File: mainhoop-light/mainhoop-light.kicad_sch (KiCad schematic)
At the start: 69 parts, among them IC1 BCR420U, IC3 BCR420U, IC4 BCR420U, IC5 BCR420U, IC6 BCR420U, J1 Conn_01x04, Q1 2N7002, Q12 Si2301CDS, Q13 2N7002, Q14 2N7002, Q15 Si2301CDS, Q16 2N7002, Q2 2N7002, Q3 Si2301CDS, Q7 2N7002, U1 AP2204K-ADJ, U2 SE555D

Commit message: Add files via upload
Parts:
- added R11, R12, R13: 10k, Resistor_SMD:R_0603_1608Metric, symbol Device:R_Small
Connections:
- net GND: now also R11.1, R12.1, R13.1
- net GREEN_EN: now also R11.2
- net RED_EN: now also R12.2
- net at Q2.1 (G): now also Q1.3 (D), R1.1
- net TSAL renamed RTML
- net TSAL_EN renamed RTML_EN
- net RTML_EN: now also R13.2
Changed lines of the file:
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@@
     (company "NCKU Formula Racing")
   )
+  (junction (at 200.66 152.4) (diameter 0) (color 0 0 0 0)
+  )
   (junction (at 59.055 35.56) (diameter 0) (color 0 0 0 0)
   )
@@
   (junction (at 69.85 41.91) (diameter 0) (color 0 0 0 0)
   )
+  (junction (at 171.45 152.4) (diameter 0) (color 0 0 0 0)
+  )
+  (junction (at 200.66 125.73) (diameter 0) (color 0 0 0 0)
+  )
   (junction (at 67.945 76.835) (diameter 0) (color 0 0 0 0)
   )
@@
   (junction (at 67.945 70.485) (diameter 0) (color 0 0 0 0)
   )
+  (junction (at 71.12 184.15) (diameter 0) (color 0 0 0 0)
+  )
   (junction (at 40.005 135.255) (diameter 0) (color 0 0 0 0)
   )
@@
     (stroke (width 0) (type default))
   )
+  (wire (pts (xy 171.45 152.4) (xy 162.56 152.4))
+    (stroke (width 0) (type default))
+  )
   (wire (pts (xy 211.455 48.26) (xy 211.455 53.34))
     (stroke (width 0) (type default))
@@
     (stroke (width 0) (type default))
   )
+  (wire (pts (xy 220.98 152.4) (xy 200.66 152.4))
+    (stroke (width 0) (type default))
+  )
   (wire (pts (xy 198.12 71.755) (xy 198.12 74.295))
     (stroke (width 0) (type default))
@@
     (stroke (width 0) (type default))
   )
+  (wire (pts (xy 220.98 137.16) (xy 220.98 152.4))
+    (stroke (width 0) (type default))
+  )
   (wire (pts (xy 211.455 97.79) (xy 211.455 102.87))
     (stroke (width 0) (type default))
@@
     (stroke (width 0) (type default))
   )
+  (wire (pts (xy 171.45 137.16) (xy 171.45 152.4))
+    (stroke (width 0) (type default))
+  )
   (wire (pts (xy 200.66 116.84) (xy 212.09 116.84))
     (stroke (width 0) (type default))
@@
     (stroke (width 0) (type default))
   )
+  (wire (pts (xy 204.47 137.16) (xy 204.47 125.73))
+    (stroke (width 0) (type default))
+  )
   (wire (pts (xy 171.45 116.84) (xy 171.45 119.38))
     (stroke (width 0) (type default))
@@
     (stroke (width 0) (type default))
   )
+  (wire (pts (xy 85.09 186.69) (xy 74.93 186.69))
+    (stroke (width 0) (type default))
+  )
   (wire (pts (xy 69.85 35.56) (xy 69.85 36.195))
     (stroke (width 0) (type default))
   )
+  (wire (pts (xy 74.93 186.69) (xy 74.93 184.15))
+    (stroke (width 0) (type default))
+  )
   (wire (pts (xy 73.025 145.415) (xy 69.85 145.415))
     (stroke (width 0) (type default))
@@
     (stroke (width 0) (type default))
   )
+  (wire (pts (xy 74.93 184.15) (xy 71.12 184.15))
+    (stroke (width 0) (type default))
+  )
   (wire (pts (xy 164.465 58.42) (xy 197.485 58.42))
     (stroke (width 0) (type default))
@@
     (stroke (width 0) (type default))
   )
+  (wire (pts (xy 204.47 125.73) (xy 200.66 125.73))
+    (stroke (width 0) (type default))
+  )
   (wire (pts (xy 67.31 45.72) (xy 69.85 45.72))
     (stroke (width 0) (type default))
   )
-  (wire (pts (xy 71.12 182.88) (xy 71.12 185.42))
+  (wire (pts (xy 71.12 182.88) (xy 71.12 184.15))
     (stroke (width 0) (type default))
   )
@@
     (stroke (width 0) (type default))
   )
+  (wire (pts (xy 71.12 184.15) (xy 71.12 185.42))
+    (stroke (width 0) (type default))
+  )
   (wire (pts (xy 167.005 49.53) (xy 164.465 49.53))
     (stroke (width 0) (type default))
@@
     (stroke (width 0) (type default))
   )
-  (wire (pts (xy 200.66 152.4) (xy 162.56 152.4))
+  (wire (pts (xy 200.66 152.4) (xy 171.45 152.4))
     (stroke (width 0) (type default))
   )
@@
     (effects (font (size 1.27 1.27)) (justify left bottom))
   )
-  (global_label "TSAL" (shape input) (at 63.5 95.25 270) (fields_autoplaced)
+  (global_label "RTML" (shape input) (at 63.5 95.25 270) (fields_autoplaced)
     (effects (font (size 1.27 1.27)) (justify right))
-    (property "Intersheetrefs" "${INTERSHEET_REFS}" (at 63.5 102.529 90)
-      (effects (font (size 1.27 1.27)) (justify left) hide)
+    (property "Intersheetrefs" "${INTERSHEET_REFS}" (at 63.5 102.9523 90)
+      (effects (font (size 1.27 1.27)) (justify right) hide)
     )
   )
@@
     )
   )
-  (global_label "TSAL_EN" (shape input) (at 171.45 132.08 0) (fields_autoplaced)
+  (global_label "RTML_EN" (shape input) (at 171.45 132.08 0) (fields_autoplaced)
     (effects (font (size 1.27 1.27)) (justify left))
-    (property "Intersheetrefs" "${INTERSHEET_REFS}" (at 182.1761 132.08 0)
+    (property "Intersheetrefs" "${INTERSHEET_REFS}" (at 182.5994 132.08 0)
       (effects (font (size 1.27 1.27)) (justify left) hide)
     )
@@
     )
   )
-  (global_label "TSAL" (shape input) (at 143.51 130.81 180) (fields_autoplaced)
+  (global_label "RTML" (shape input) (at 143.51 130.81 180) (fields_autoplaced)
     (effects (font (size 1.27 1.27)) (justify right))
-    (property "Intersheetrefs" "${INTERSHEET_REFS}" (at 136.231 130.81 0)
+    (property "Intersheetrefs" "${INTERSHEET_REFS}" (at 135.8077 130.81 0)
       (effects (font (size 1.27 1.27)) (justify right) hide)
     )
@@
     )
   )
-  (global_label "TSAL" (shape input) (at 37.465 95.25 0) (fields_autoplaced)
+  (global_label "RTML" (shape input) (at 37.465 95.25 0) (fields_autoplaced)
     (effects (font (size 1.27 1.27)) (justify left))
-    (property "Intersheetrefs" "${INTERSHEET_REFS}" (at 44.744 95.25 0)
+    (property "Intersheetrefs" "${INTERSHEET_REFS}" (at 45.1673 95.25 0)
       (effects (font (size 1.27 1.27)) (justify left) hide)
     )
   )
-  (global_label "TSAL_EN" (shape input) (at 67.945 65.405 0) (fields_autoplaced)
+  (global_label "RTML_EN" (shape input) (at 67.945 65.405 0) (fields_autoplaced)
     (effects (font (size 1.27 1.27)) (justify left))
-    (property "Intersheetrefs" "${INTERSHEET_REFS}" (at 78.6711 65.405 0)
+    (property "Intersheetrefs" "${INTERSHEET_REFS}" (at 79.0944 65.405 0)
       (effects (font (size 1.27 1.27)) (justify left) hide)
     )
@@
     )
   )
+  (symbol (lib_id "Device:R_Small") (at 85.09 184.15 180) (unit 1)
+    (in_bom yes) (on_board yes) (dnp no) (fields_autoplaced)
+    (property "Reference" "R11" (at 83.185 185.42 0)
+      (effects (font (size 1.27 1.27)) (justify left))
+    )
+    (property "Value" "10k" (at 83.185 182.88 0)
+      (effects (font (size 1.27 1.27)) (justify left))
+    )
+    (property "Footprint" "Resistor_SMD:R_0603_1608Metric" (at 85.09 184.15 0)
+      (effects (font (size 1.27 1.27)) hide)
+    )
+    (property "Datasheet" "~" (at 85.09 184.15 0)
+      (effects (font (size 1.27 1.27)) hide)
+    )
+    (pin "1")
+    (pin "2")
+    (instances
+      (project "mainhoop-light"
+        (path "/e305e7a0-e5ef-41c9-b477-d7eaddabcdca"
+          (reference "R11") (unit 1)
+        )
+      )
+    )
+  )
   (symbol (lib_id "Device:R_Small") (at 151.13 123.19 180) (unit 1)
     (in_bom yes) (on_board yes) (dnp no) (fields_autoplaced)
@@
     )
   )
+  (symbol (lib_id "Device:R_Small") (at 171.45 134.62 180) (unit 1)
+    (in_bom yes) (on_board yes) (dnp no) (fields_autoplaced)
+    (property "Reference" "R13" (at 169.545 135.89 0)
+      (effects (font (size 1.27 1.27)) (justify left))
+    )
+    (property "Value" "10k" (at 169.545 133.35 0)
+      (effects (font (size 1.27 1.27)) (justify left))
+    )
+    (property "Footprint" "Resistor_SMD:R_0603_1608Metric" (at 171.45 134.62 0)
+      (effects (font (size 1.27 1.27)) hide)
+    )
+    (property "Datasheet" "~" (at 171.45 134.62 0)
+      (effects (font (size 1.27 1.27)) hide)
+    )
+    (pin "1")
+    (pin "2")
+    (instances
+      (project "mainhoop-light"
+        (path "/e305e7a0-e5ef-41c9-b477-d7eaddabcdca"
+          (reference "R13") (unit 1)
+        )
+      )
+    )
+  )
   (symbol (lib_id "power:GND") (at 40.005 141.605 0) (unit 1)
     (in_bom yes) (on_board yes) (dnp no) (fields_autoplaced)
@@
         )
       )
+    )
+  )
+  (symbol (lib_id "Device:R_Small") (at 220.98 134.62 180) (unit 1)
+    (in_bom yes) (on_board yes) (dnp no) (fields_autoplaced)
+    (property "Reference" "R12" (at 219.075 135.89 0)
+      (effects (font (size 1.27 1.27)) (justify left))
+    )
+    (property "Value" "10k" (at 219.075 133.35 0)
+      (effects (font (size 1.27 1.27)) (justify left))
+    )
+    (property "Footprint" "Resistor_SMD:R_0603_1608Metric" (at 220.98 134.62 0)
+      (effects (font (size 1.27 1.27)) hide)
+    )
+    (property "Datasheet" "~" (at 220.98 134.62 0)
+      (effects (font (size 1.27 1.27)) hide)
+    )
+    (pin "1")
+    (pin "2")
+    (instances
+      (project "mainhoop-light"
+        (path "/e305e7a0-e5ef-41c9-b477-d7eaddabcdca"
+          (reference "R12") (unit 1)
+        )
+      )

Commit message: change the pads' size
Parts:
- H1, H2: footprint MountingHole:MountingHole_6.4mm_M6_DIN965_Pad_TopBottom -> MountingHole:MountingHole_4mm_Pad_TopBottom
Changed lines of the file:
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@@
       (effects (font (size 1.27 1.27)) (justify left))
     )
-    (property "Footprint" "MountingHole:MountingHole_6.4mm_M6_DIN965_Pad_TopBottom" (at 81.28 43.815 0)
+    (property "Footprint" "MountingHole:MountingHole_4mm_Pad_TopBottom" (at 81.28 43.815 0)
       (effects (font (size 1.27 1.27)) hide)
     )
@@
       (effects (font (size 1.27 1.27)) (justify left))
     )
-    (property "Footprint" "MountingHole:MountingHole_6.4mm_M6_DIN965_Pad_TopBottom" (at 81.28 30.48 0)
-      (effects (font (size 1.27 1.27)) hide)
-    )
+    (property "Footprint" "MountingHole:MountingHole_4mm_Pad_TopBottom" (at 81.28 30.48 0)
+      (effects (font (size 1.27 1.27)) hide)
+    )

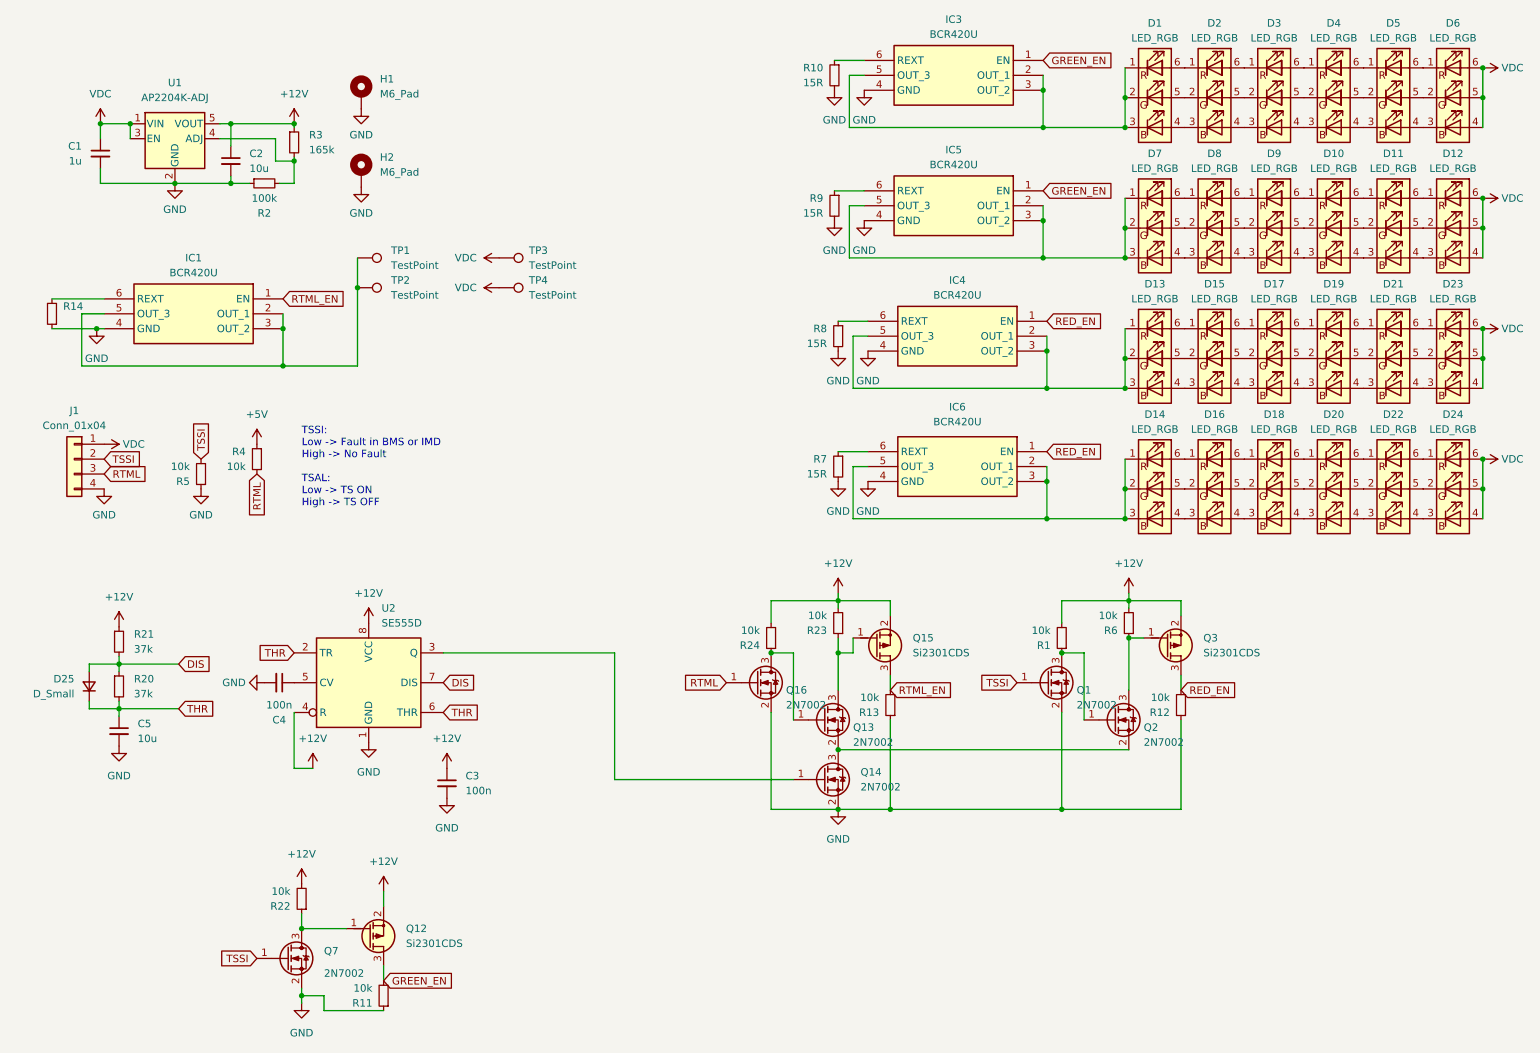
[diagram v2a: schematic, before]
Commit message: fix: replace PMOS, resistor and pull-up of RTML
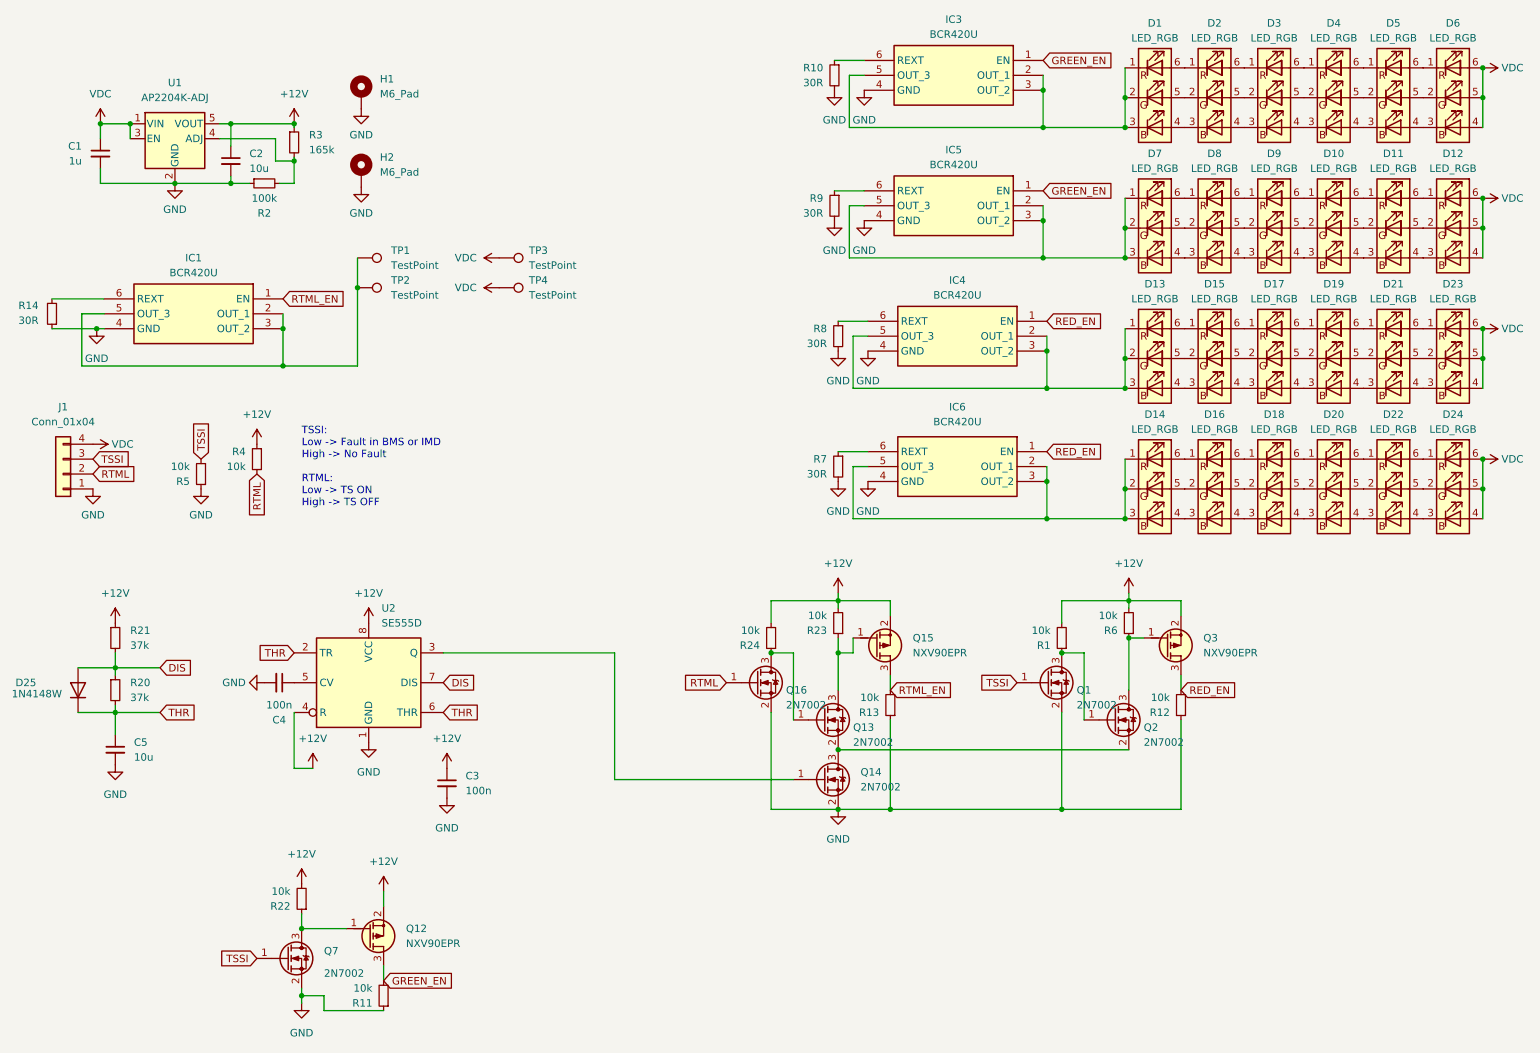
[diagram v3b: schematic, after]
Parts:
- removed D25: D_Small, Diode_SMD:D_SOD-123F, symbol Device:D_Small
- added D25: 1N4148W, Diode_SMD:D_SOD-123, symbol Diode:1N4148W
- J1: footprint Connector_Wuerth:Wuerth_WR-WTB_64800411622_1x04_P1.50mm_Vertical -> Connector_JST:JST_XH_B4B-XH-A_1x04_P2.50mm_Vertical
- Q12, Q15, Q3: value Si2301CDS -> NXV90EPR; footprint Package_TO_SOT_SMD:SOT-23 -> Package_TO_SOT_SMD:SOT-23-3
- R10, R7, R8, R9: value 15R -> 30R
- R14: value ~ -> 30R
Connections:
- net +5V is gone; now on net +12V: R4.1
- net DIS: now also D25.2 (A)
- net GND: now also J1.1 (Pin_1); no longer J1.4 (Pin_4)
- net RTML: now also J1.2 (Pin_2); no longer J1.3 (Pin_3)
- net THR: now also D25.1 (K)
- net TSSI: now also J1.3 (Pin_3); no longer J1.2 (Pin_2)
- net VDC: now also J1.4 (Pin_4); no longer J1.1 (Pin_1)
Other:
- note added: "TSSI: Low -> Fault in BMS or IMD High -> No Fault RTML: Low -> TS ON High -> TS OFF"
- note removed: "TSSI: Low -> Fault in BMS or IMD High -> No Fault TSAL: Low -> TS ON High -> TS OFF"
- moved on the sheet: C5, R20, R21
